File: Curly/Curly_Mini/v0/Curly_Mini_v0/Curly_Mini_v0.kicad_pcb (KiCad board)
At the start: 4 copper layers, 44.5 x 20.3 mm, 51 parts, among them J1 DEBUG_PORT, J26 Conn_01x24_Pin, J8 SHORT_USB, U1 RP2040, U2 MCP25625T-E_ML, U3 XC6206PxxxMR, U4 W25Q16JVUXIQ_TR, U5 SE8650X2-HF, U6 MAX3232, Y2 12.000 MHz, C9002

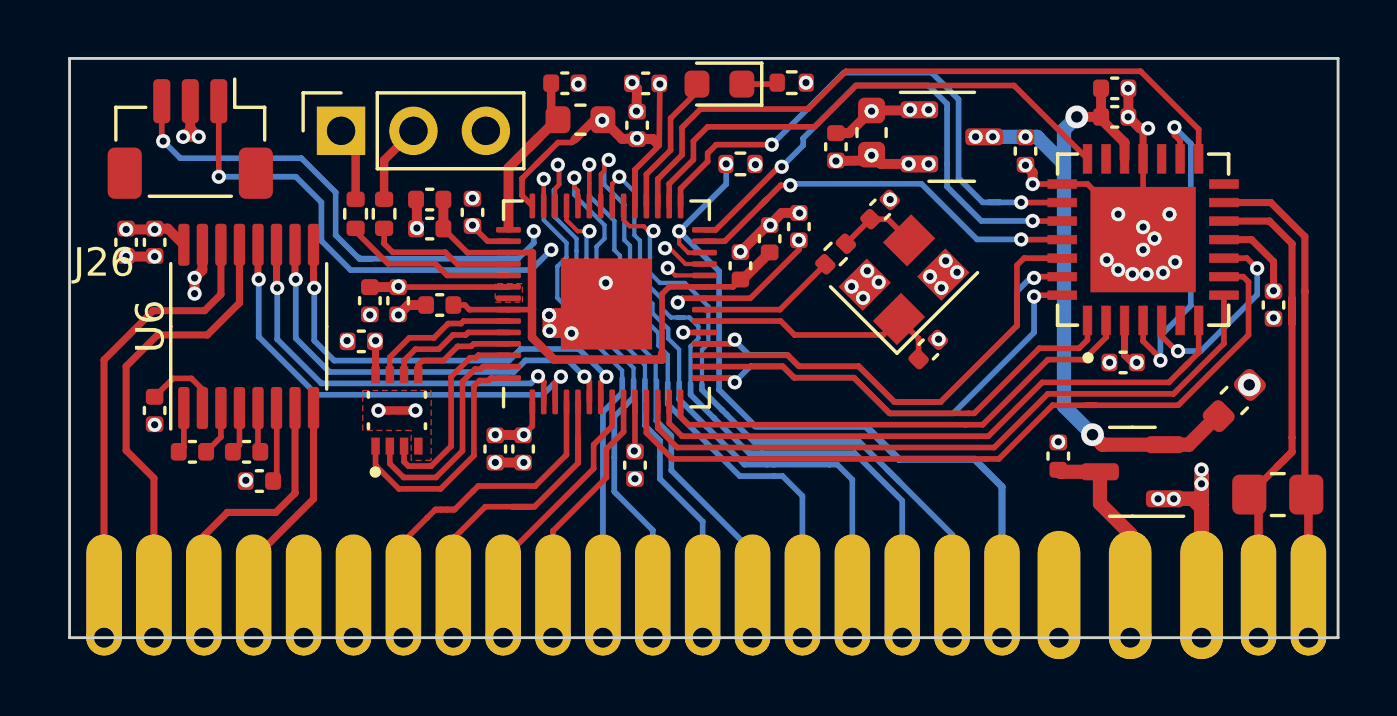
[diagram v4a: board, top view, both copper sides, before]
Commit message: Final v0 revision made, JLC fab files provided. Castellated holes are ultra expensive, moved to 2 sided edge connect
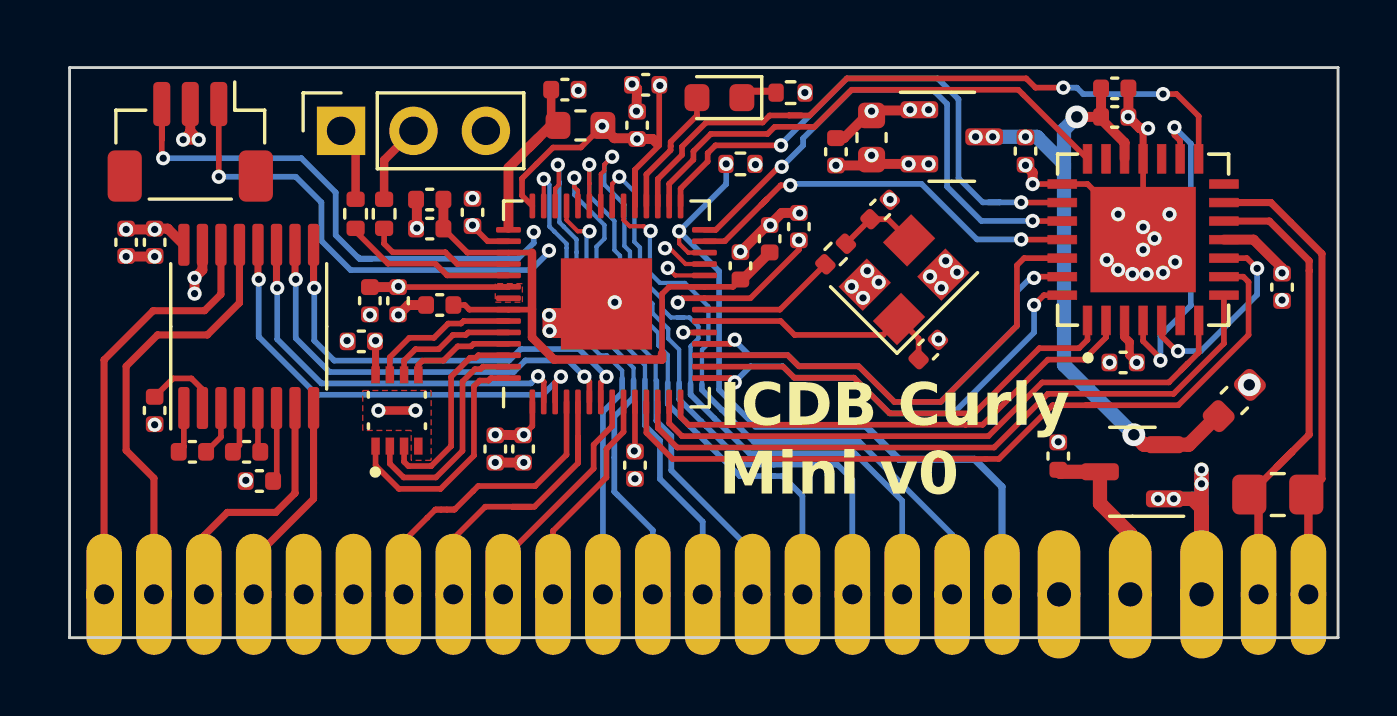
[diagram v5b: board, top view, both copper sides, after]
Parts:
- R1: value 4k7 -> 5k1
- moved J26 1.52 mm to (70.4, 69.6)
- moved C27 0.69 mm to (111.8, 58.8)
- moved D1 0.47 mm to (92.0, 52.2)
- moved R5 0.35 mm to (94.5, 52.0)
- moved C4 0.23 mm to (86.6, 51.9)
- moved FB1 0.20 mm to (87.1, 53.1)
- moved C20 0.18 mm to (97.3, 53.6)
- moved C21 0.18 mm to (96.1, 54.1)
- moved J1 0.10 mm to (73.5, 53.7)
- moved C15 0.05 mm to (89.4, 51.7)
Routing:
- net /SWDIO: track 24.5 -> 26.1 mm
- net +3V3: track 43.1 -> 44.0 mm
- net +5V: track 24.0 -> 23.2 mm
- net GND: track 56.5 -> 56.9 mm, vias 68 -> 65
- net /CAN_TXVR_STBY: track 23.9 -> 24.1 mm, vias 0 -> 2
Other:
- board size 44.5 x 20.3 mm -> 44.5 x 20 mm
- board text added: "CURLY MINI"
- board text added: "ICDB Curly Mini v0"
- board text added: "Joseph A. De Vico 01/01/2024"

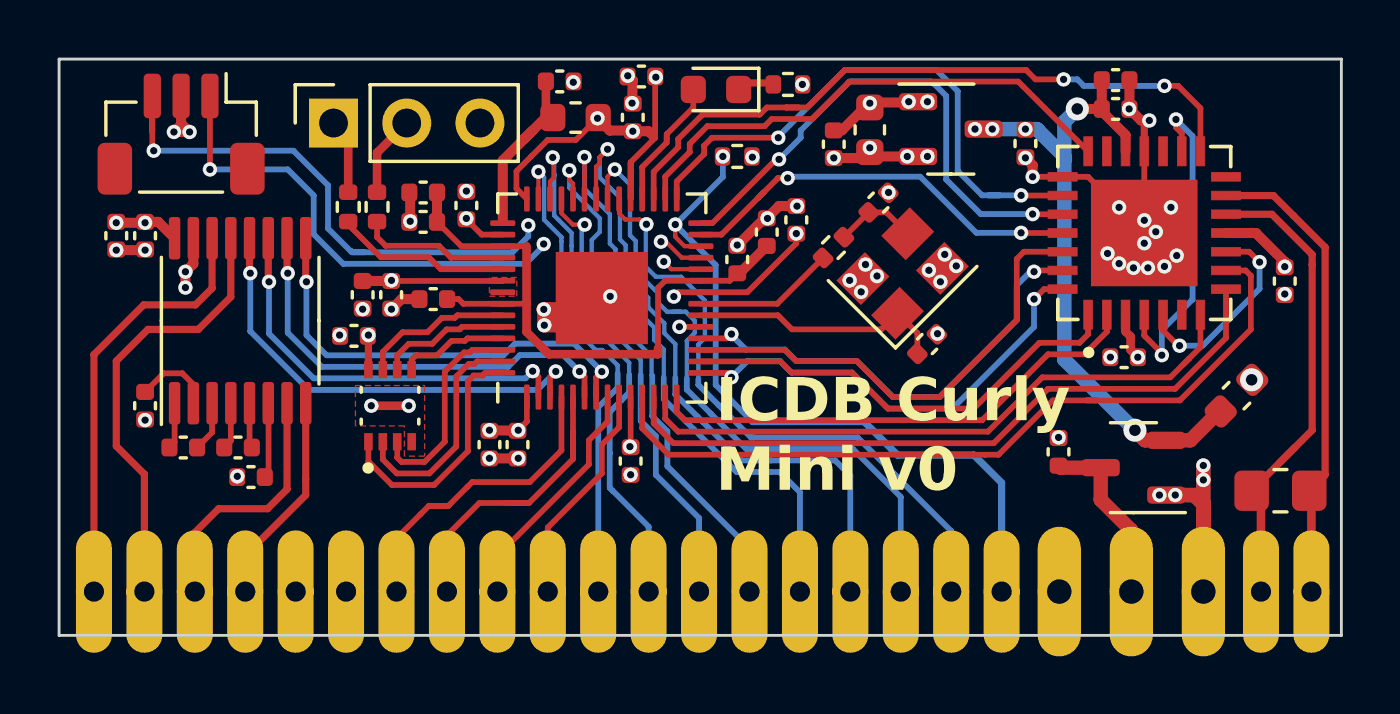
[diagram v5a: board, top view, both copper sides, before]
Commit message: Added USB ESD Protection, USB Boot button - Curly
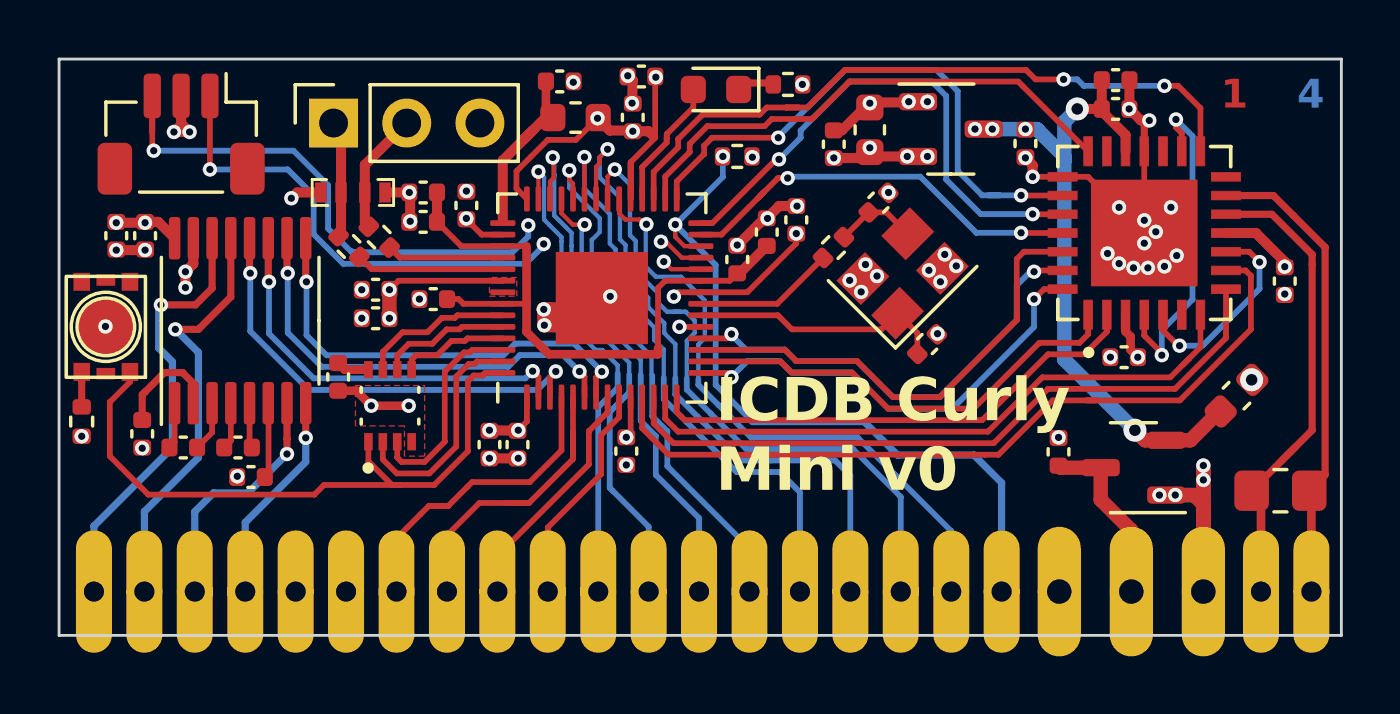
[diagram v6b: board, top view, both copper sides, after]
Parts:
- added D2: ACPDQC3V3T-HF, ICDB_Curly:0402C-SOD-923F, F.Cu at (80.2, 55.8)
- added D3: ACPDQC3V3T-HF, ICDB_Curly:0402C-SOD-923F, F.Cu at (78.7, 55.8)
- added R7: 10k, Resistor_SMD:R_0402_1005Metric, F.Cu at (70.0, 63.7)
- added SW1: SW_SPST, ICDB_Curly:TPS850 J14Q V SMTR LFS, F.Cu at (70.8, 60.4)
- added TP1: TestPoint, TestPoint:TestPoint_Pad_D2.0mm, F.Cu at (70.8, 60.4)
- moved C1 1.53 mm to (78.9, 62.1), turned to -90 degrees
- moved R3 1.38 mm to (79.3, 57.6), turned to -45 degrees
- moved R4 1.05 mm to (80.3, 57.3), turned to -45 degrees
- moved C32 0.98 mm to (72.1, 64.1)
- moved C14 0.98 mm to (80.2, 60.1), turned to 180 degrees
- moved C13 0.48 mm to (80.2, 59.1), turned to 180 degrees
- moved C18 0.38 mm to (88.9, 64.7)
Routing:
- net /~{QSPI_CSN}: track 8.72 -> 22.7 mm
- net /RS232_0_RX: track 16.9 -> 14.6 mm, vias 0 -> 1
- net GND: track 56.9 -> 59.1 mm, vias 65 -> 69
- net /USB_DP: track 2.61 -> 4.79 mm
- net /RS232_1_TX: track 10.4 -> 8.57 mm, vias 0 -> 1
- net /RS232_0_TX: track 16.9 -> 15.4 mm, vias 0 -> 1
- net /USB_DM: track 2.83 -> 4.26 mm
- net +3V3: track 44.0 -> 42.6 mm
- net Net-(U1-USB_DM): track 5.34 -> 4.07 mm
- net /RS232_1_RX: track 8.75 -> 10.0 mm, vias 0 -> 1
- net Net-(SW1-B): track 0.00 -> 1.21 mm
- net Net-(U6-VS+): track 2.75 -> 3.81 mm
- net Net-(U1-USB_DP): track 6.11 -> 5.15 mm
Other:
- board text added: "1"
- board text added: "2"
- board text added: "3"
- board text added: "4"

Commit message: Small cleanup on Curly
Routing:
- net +3V3: track 42.6 -> 44.7 mm
- net /RS232_0_RX: track 14.6 -> 13.5 mm
- net /RS232_0_TX: track 15.4 -> 14.3 mm
- net /~{EXT_RESET}: track 27.3 -> 28.2 mm
- net /CANL: track 18.5 -> 17.8 mm
- net +1V1: track 22.0 -> 22.6 mm, vias 0 -> 3
- net /CANH: track 18.0 -> 18.5 mm
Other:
- board text added: "Rev. 2"
